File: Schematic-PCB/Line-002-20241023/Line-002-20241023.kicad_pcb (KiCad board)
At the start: 2 copper layers, 195 x 192.8 mm, 217 parts, among them U53 ATmega2560-16A

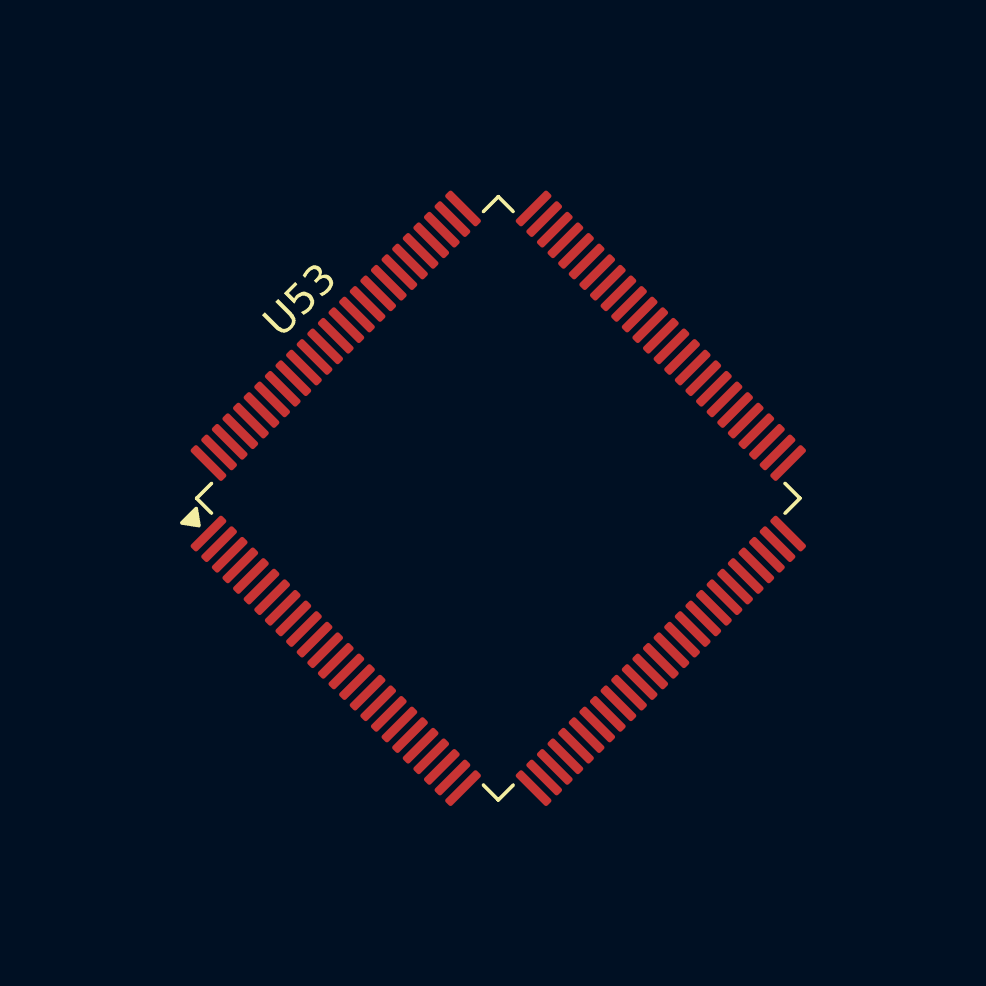
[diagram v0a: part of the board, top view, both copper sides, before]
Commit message: update: ラインセンサ ver.002 の回路図を進めた
コンパレータを追加
ピンアサインはちょっと悩み中だけどほぼいい感じだと思う...たぶん。
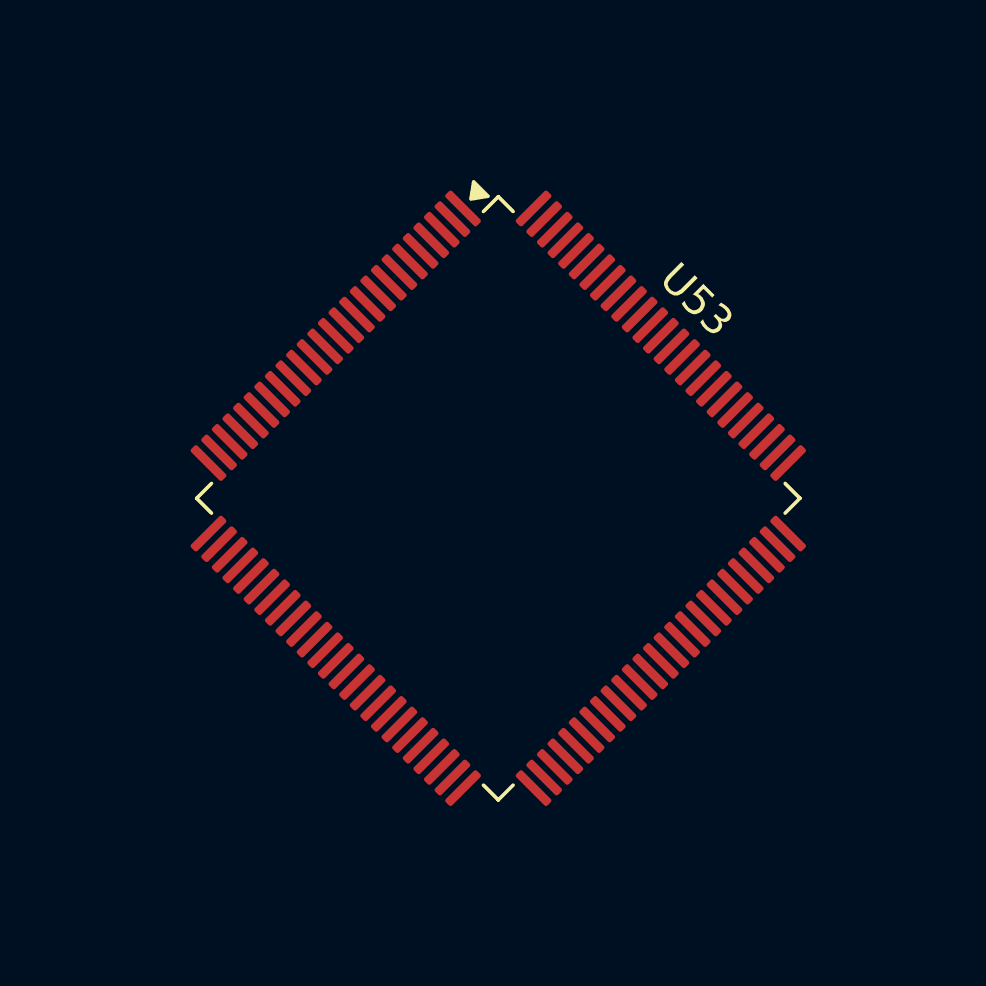
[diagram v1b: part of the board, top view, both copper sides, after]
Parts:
- turned U53 to -45 degrees

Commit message: add: update: ラインセンサ基板の外形の更新版を追加 & PCBデザイン/回路図を進めた
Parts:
- removed R100, R101, R102, R103, R104, R92, R93, R94, R95, R96, R97, R98, R99: 75, Resistor_SMD:R_0603_1608Metric
- removed R105: 10K, Resistor_SMD:R_0603_1608Metric
- removed R106, R107, R108: 330, Resistor_SMD:R_0603_1608Metric
- removed U46, U47, U48, U49, U50, U51, U52: ~, @2024TOINIOT2-Line:NJL7502L
- removed U53: ATmega2560-16A, Package_QFP:TQFP-100_14x14mm_P0.5mm
- added C1: 100nF, Capacitor_SMD:C_0603_1608Metric, F.Cu at (203.2, 62.1)
- added C2: 100nF, Capacitor_SMD:C_0603_1608Metric, F.Cu at (203.2, 64.6)
- added C3: 22pF, Capacitor_SMD:C_0603_1608Metric, F.Cu at (203.2, 67.1)
- added C4: 22pF, Capacitor_SMD:C_0603_1608Metric, F.Cu at (203.2, 69.6)
- added C5: 100nF, Capacitor_SMD:C_0603_1608Metric, F.Cu at (203.2, 72.1)
- added C6: 22pF, Capacitor_SMD:C_0603_1608Metric, F.Cu at (203.2, 74.6)
- added C7: 100nF, Capacitor_SMD:C_0603_1608Metric, F.Cu at (203.2, 77.1)
- added C8: 1000uF, Capacitor_SMD:C_0603_1608Metric, F.Cu at (203.2, 79.7)
- added C9: 10uF, Capacitor_SMD:C_0805_2012Metric, F.Cu at (203.5, 110.7)
- added D56: PWR, LED_SMD:LED_0603_1608Metric, F.Cu at (229.5, 113.2)
- added J1: ICSP, Connector_PinHeader_2.54mm:PinHeader_2x03_P2.54mm_Vertical, F.Cu at (249.7, 106.4)
- added J2: VIN, Connector_JST:JST_VH_B2P-VH-B_1x02_P3.96mm_Vertical, F.Cu at (-12.0, 29.9)
- added JP1: 160Hz, Jumper:SolderJumper-2_P1.3mm_Open_Pad1.0x1.5mm, F.Cu at (229.7, 95.2)
- added JP2: 16Hz, Jumper:SolderJumper-2_P1.3mm_Open_Pad1.0x1.5mm, F.Cu at (229.7, 98.8)
- added JP3: 1.6Hz, Jumper:SolderJumper-2_P1.3mm_Open_Pad1.0x1.5mm, F.Cu at (229.7, 102.3)
- added Y1: 16MHz, @2024TOINIOT2-Line:AL4BT, F.Cu at (239.4, 110.5)
- D25, D26, D27, D28, D29, U25, U26, U27, U28, U29: moved to B.Cu
- R29, R30, R31, R32, R33, R34, R35, R36, R37, R38, R39, R40, R41, R42, R43, R44, R45, R46, R47, R48, R49, R50, R51, R52: value Line-PDWN -> 75
- R81, R82, R87, R90: value 75 -> 10K
- R83, R84, R85, R91: value 75 -> 330
- R86: value 75 -> 1M
- R88: value 75 -> 100
- R89: value 75 -> 1K
- U45: value ~ -> ATmega2560-16A; footprint @2024TOINIOT2-Line:NJL7502L -> Package_QFP:TQFP-100_14x14mm_P0.5mm
- moved U25 283.0 mm to (-22.5, -87.4), turned to 50 degrees
- moved U26 275.2 mm to (-12.0, -81.3), turned to 70 degrees
- moved U27 269.7 mm to (-0.00, -79.2), turned to 90 degrees
- moved U29 236.8 mm to (22.5, -87.4), turned to 130 degrees
- moved U28 235.7 mm to (12.0, -81.3), turned to 110 degrees
- moved D25 215.3 mm to (-25.7, -83.5), turned to -130 degrees
- moved D26 206.7 mm to (-13.7, -76.6), turned to -110 degrees
- moved D27 201.4 mm to (-0.00, -74.2), turned to -90 degrees
- moved U45 196.4 mm to (7.50, 41.0), turned to -45 degrees
- moved D29 166.2 mm to (25.7, -83.5), turned to -50 degrees
- moved D28 163.1 mm to (13.7, -76.6), turned to -70 degrees
- moved D36 129.8 mm to (241.5, 63.5)
- moved D42 126.9 mm to (246.9, 63.5)
- moved D43 126.9 mm to (246.9, 69.0)
- moved D44 126.9 mm to (246.9, 74.5)
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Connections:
- R25 pad 1: Line-F-01 -> Line-F
- R26 pad 1: Line-F-02 -> Line-L
- R27 pad 1: Line-F-03 -> Line-B
- R28 pad 1: Line-F-04 -> Line-R
- R29 pad 1: Line-F-05 -> +5V
- R29 pad 2: GND -> Net-(D1-A)
- R30 pad 1: Line-F-06 -> +5V
- R30 pad 2: GND -> Net-(D2-A)
- R31 pad 1: Line-F-07 -> +5V
- R31 pad 2: GND -> Net-(D3-A)
- R32 pad 1: Line-L-01 -> +5V
- R32 pad 2: GND -> Net-(D4-A)
- R33 pad 1: Line-L-02 -> +5V
- R33 pad 2: GND -> Net-(D5-A)
- R34 pad 1: Line-L-03 -> +5V
- R34 pad 2: GND -> Net-(D6-A)
- R35 pad 1: Line-L-04 -> +5V
- R35 pad 2: GND -> Net-(D7-A)
- R36 pad 1: Line-L-05 -> +5V
- R36 pad 2: GND -> Net-(D8-A)
- R37 pad 1: Line-L-06 -> +5V
- R37 pad 2: GND -> Net-(D9-A)
- R38 pad 1: Line-L-07 -> +5V
- R38 pad 2: GND -> Net-(D10-A)
- R39 pad 1: Line-B-01 -> +5V
- R39 pad 2: GND -> Net-(D11-A)
- R40 pad 1: Line-B-02 -> +5V
- R40 pad 2: GND -> Net-(D12-A)
- R41 pad 1: Line-B-03 -> +5V
- R41 pad 2: GND -> Net-(D13-A)
- R42 pad 1: Line-B-04 -> +5V
- R42 pad 2: GND -> Net-(D14-A)
- R43 pad 1: Line-B-05 -> +5V
- R43 pad 2: GND -> Net-(D15-A)
- R44 pad 1: Line-B-06 -> +5V
- R44 pad 2: GND -> Net-(D16-A)
- R45 pad 1: Line-B-07 -> +5V
- R45 pad 2: GND -> Net-(D17-A)
- R46 pad 1: Line-R-01 -> +5V
- R46 pad 2: GND -> Net-(D18-A)
- R47 pad 1: Line-R-02 -> +5V
- R47 pad 2: GND -> Net-(D19-A)
- R48 pad 1: Line-R-03 -> +5V
- R48 pad 2: GND -> Net-(D20-A)
- R49 pad 1: Line-R-04 -> +5V
- R49 pad 2: GND -> Net-(D21-A)
- R50 pad 1: Line-R-05 -> +5V
- R50 pad 2: GND -> Net-(D22-A)
- R51 pad 1: Line-R-06 -> +5V
- R51 pad 2: GND -> Net-(D23-A)
- R52 pad 1: Line-R-07 -> +5V
- R52 pad 2: GND -> Net-(D24-A)
- R53 pad 2: Net-(D1-A) -> Net-(D25-A)
- R54 pad 2: Net-(D2-A) -> Net-(D26-A)
- R55 pad 2: Net-(D3-A) -> Net-(D27-A)
- R56 pad 2: Net-(D4-A) -> Net-(D28-A)
- R57 pad 2: Net-(D5-A) -> Net-(D29-A)
- R58 pad 2: Net-(D6-A) -> Net-(D30-A)
- R59 pad 2: Net-(D7-A) -> Net-(D31-A)
- R60 pad 2: Net-(D8-A) -> Net-(D32-A)
- R61 pad 2: Net-(D9-A) -> Net-(D33-A)
- R62 pad 2: Net-(D10-A) -> Net-(D34-A)
- R63 pad 2: Net-(D11-A) -> Net-(D35-A)
- R64 pad 2: Net-(D12-A) -> Net-(D36-A)
- R65 pad 2: Net-(D13-A) -> Net-(D37-A)
- R66 pad 2: Net-(D14-A) -> Net-(D38-A)
- R67 pad 2: Net-(D15-A) -> Net-(D39-A)
- R68 pad 2: Net-(D16-A) -> Net-(D40-A)
- R69 pad 2: Net-(D17-A) -> Net-(D41-A)
- R70 pad 2: Net-(D18-A) -> Net-(D42-A)
- R71 pad 2: Net-(D19-A) -> Net-(D43-A)
- R72 pad 2: Net-(D20-A) -> Net-(D44-A)
- R73 pad 2: Net-(D21-A) -> Net-(D45-A)
- R74 pad 2: Net-(D22-A) -> Net-(D46-A)
- R75 pad 2: Net-(D23-A) -> Net-(D47-A)
- R76 pad 2: Net-(D24-A) -> Net-(D48-A)
- R77 pad 2: Net-(D25-A) -> Net-(D49-A)
- R78 pad 2: Net-(D26-A) -> Net-(D50-A)
- R79 pad 2: Net-(D27-A) -> Net-(D51-A)
- R80 pad 2: Net-(D28-A) -> Net-(D52-A)
- R81 pad 2: Net-(D29-A) -> RESET
- R82 pad 2: Net-(D30-A) -> SDA
- R83 pad 1: +5V -> LED01
- R83 pad 2: Net-(D31-A) -> Net-(D53-A)
- R84 pad 1: +5V -> LED02
- R84 pad 2: Net-(D32-A) -> Net-(D54-A)
- R85 pad 1: +5V -> LED03
- R85 pad 2: Net-(D33-A) -> Net-(D55-A)
- R86 pad 1: +5V -> XTAL1
- R86 pad 2: Net-(D34-A) -> XTAL2
- R87 pad 2: Net-(D35-A) -> SCL
- R88 pad 1: +5V -> Net-(JP1-B)
- R88 pad 2: Net-(D36-A) -> Threshold
- R89 pad 1: +5V -> Net-(JP2-B)
- R89 pad 2: Net-(D37-A) -> Threshold
- R90 pad 1: +5V -> Net-(JP3-B)
- R90 pad 2: Net-(D38-A) -> Threshold
- R91 pad 1: +5V -> Net-(D56-A)
- R91 pad 2: Net-(D39-A) -> +5V
- U25 pad 1: Line-F-01 -> Line-F
- U26 pad 1: Line-F-02 -> Line-F
- U27 pad 1: Line-F-03 -> Line-F
- U28 pad 1: Line-F-04 -> Line-F
- U29 pad 1: Line-F-05 -> Line-F
- U30 pad 1: Line-F-06 -> Line-L
- U31 pad 1: Line-F-07 -> Line-L
- U32 pad 1: Line-L-01 -> Line-L
- U33 pad 1: Line-L-02 -> Line-L
- U34 pad 1: Line-L-03 -> Line-L
- U35 pad 1: Line-L-04 -> Line-B
- U36 pad 1: Line-L-05 -> Line-B
- U37 pad 1: Line-L-06 -> Line-B
- U38 pad 1: Line-L-07 -> Line-B
- U39 pad 1: Line-B-01 -> Line-B
- U40 pad 1: Line-B-02 -> Line-R
- U41 pad 1: Line-B-03 -> Line-R
- U42 pad 1: Line-B-04 -> Line-R
- U43 pad 1: Line-B-05 -> Line-R
- U44 pad 1: Line-B-06 -> Line-R
- U45 pad 1: Line-B-07 -> PWM
- U45 pad 2: +5V -> RX0
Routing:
- added copper zone on B.Cu, net GND
- added copper zone on F.Cu, net GND
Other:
- board size 195 x 192.8 mm -> 195 x 191.1 mm
- copper layers 2 -> 4

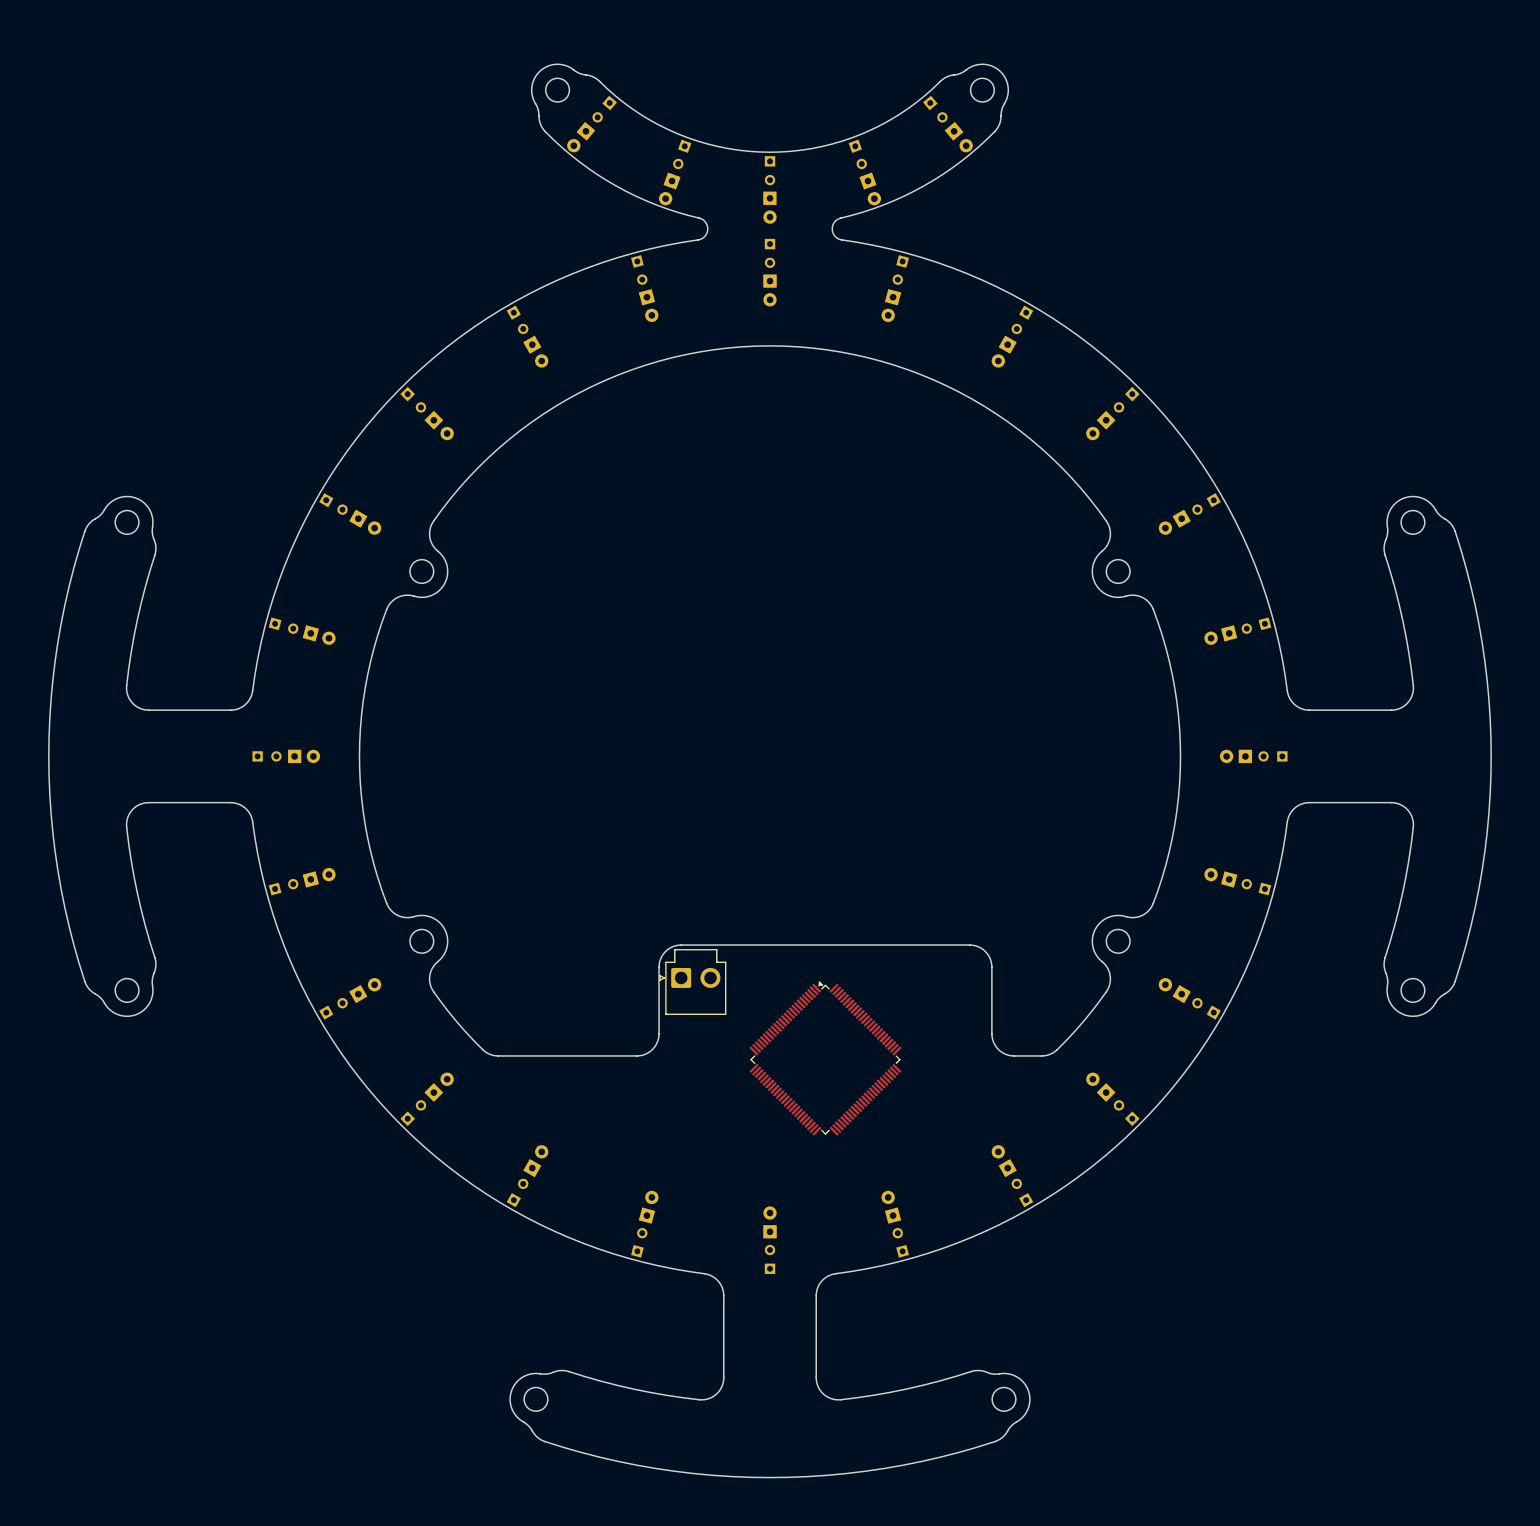
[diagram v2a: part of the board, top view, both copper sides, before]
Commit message: update: ラインセンサ基板の基板外形を更新した
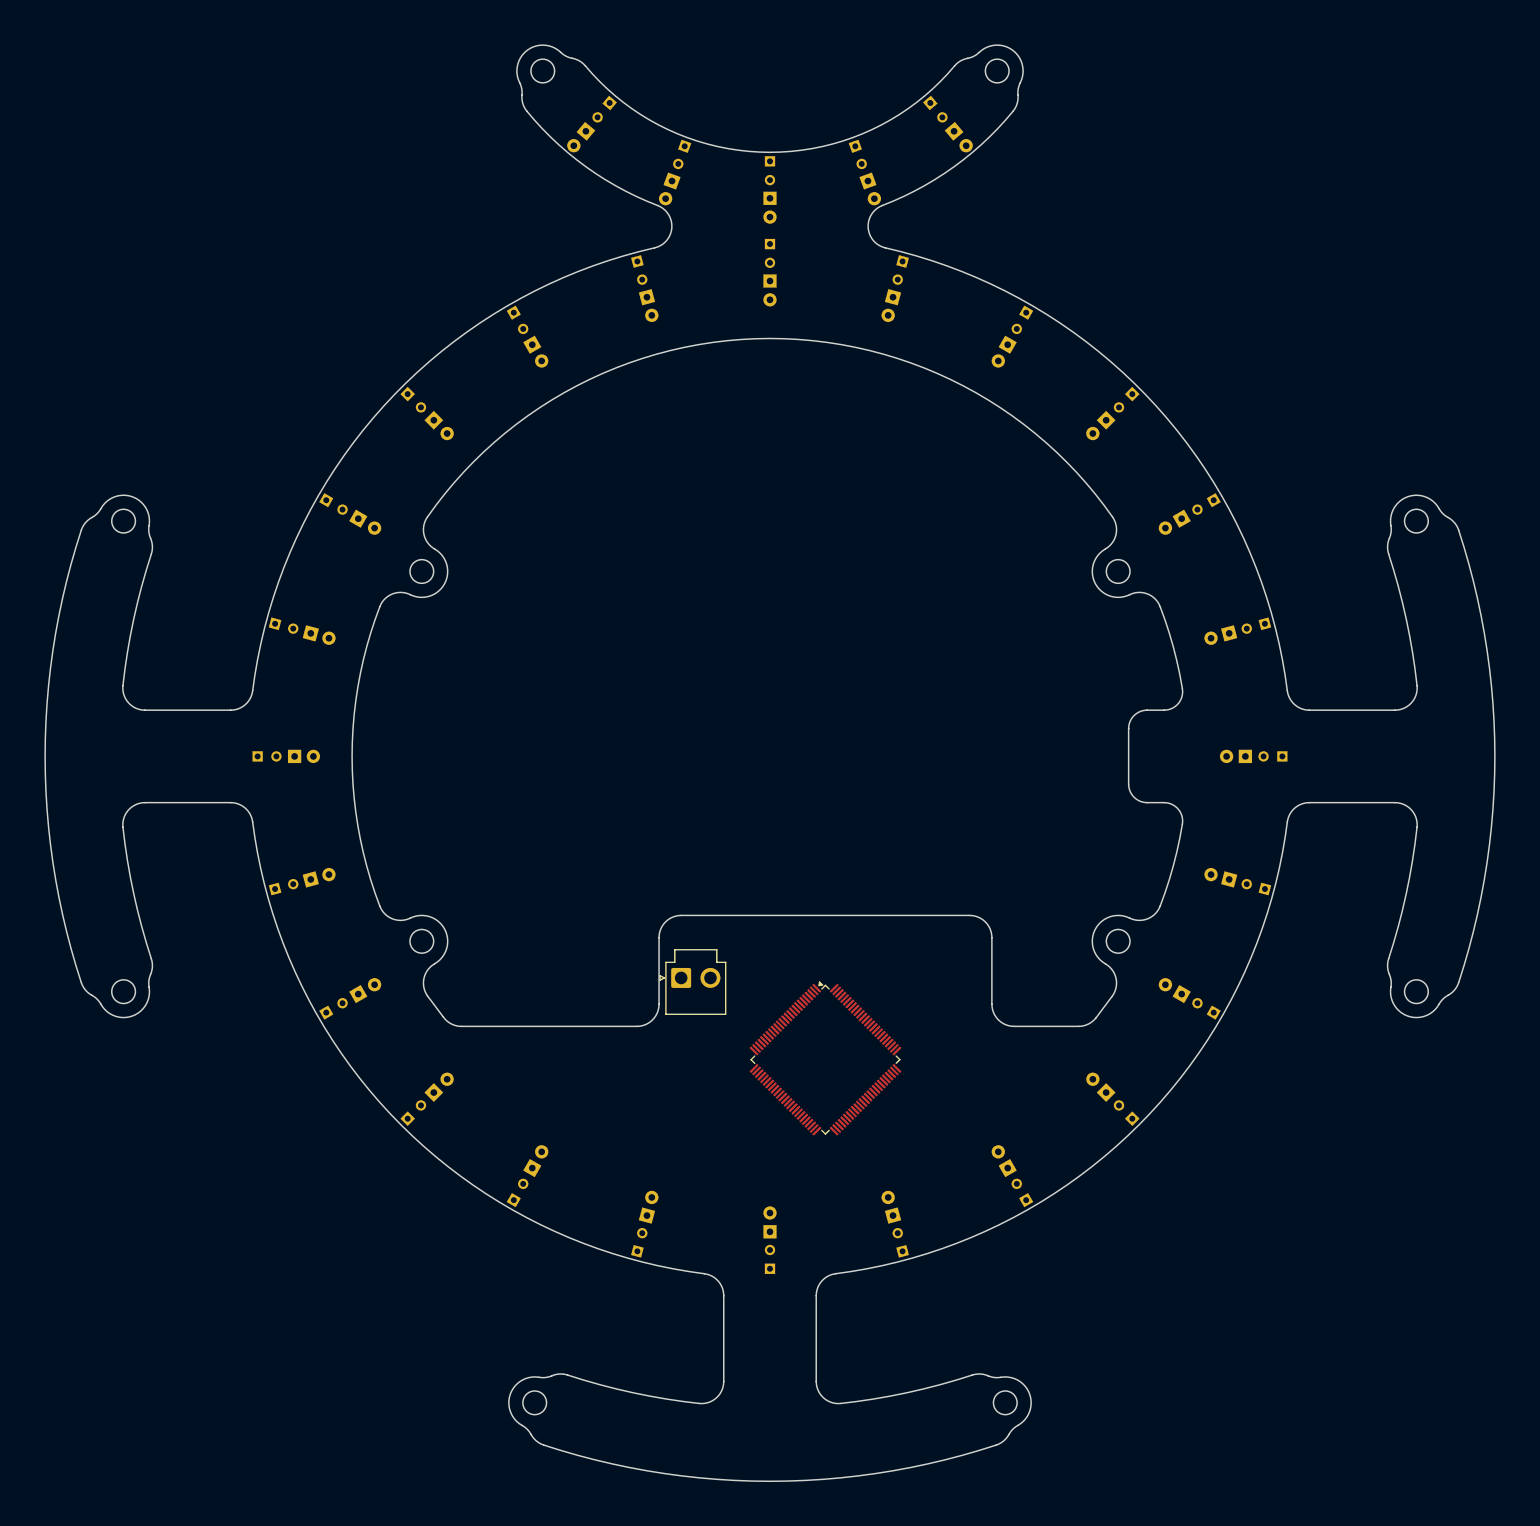
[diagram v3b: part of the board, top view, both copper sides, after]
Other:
- board size 195 x 191.1 mm -> 196 x 194.2 mm

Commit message: update: ラインセンサ基板のPCBを進めた
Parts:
- added REF**: MountingHole_3.2mm_M3, MountingHole:MountingHole_3.2mm_M3, F.Cu at (-31.8, 87.4)
- added REF**: MountingHole_3.2mm_M3, MountingHole:MountingHole_3.2mm_M3, F.Cu at (-87.4, -31.8)
- added REF**: MountingHole_3.2mm_M3, MountingHole:MountingHole_3.2mm_M3, F.Cu at (30.7, -92.7)
- added REF**: MountingHole_3.2mm_M3, MountingHole:MountingHole_3.2mm_M3, F.Cu at (87.4, -31.8)
- added REF**: MountingHole_3.2mm_M3, MountingHole:MountingHole_3.2mm_M3, F.Cu at (-30.7, -92.7)
- added REF**: MountingHole_3.2mm_M3, MountingHole:MountingHole_3.2mm_M3, F.Cu at (87.4, 31.8)
- added REF**: MountingHole_3.2mm_M3, MountingHole:MountingHole_3.2mm_M3, F.Cu at (47.1, 25.0)
- added REF**: MountingHole_3.2mm_M3, MountingHole:MountingHole_3.2mm_M3, F.Cu at (-47.1, 25.0)
- added REF**: MountingHole_3.2mm_M3, MountingHole:MountingHole_3.2mm_M3, F.Cu at (31.8, 87.4)
- added REF**: MountingHole_3.2mm_M3, MountingHole:MountingHole_3.2mm_M3, F.Cu at (-87.4, 31.8)
- added REF**: MountingHole_3.2mm_M3, MountingHole:MountingHole_3.2mm_M3, F.Cu at (-47.1, -25.0)
- moved D7 126.0 mm to (63.0, 0.00), turned to 180 degrees
- moved D19 126.0 mm to (-63.0, 0.00), turned to 0 degrees
- moved D6 121.7 mm to (60.9, -16.3), turned to -165 degrees
- moved D8 121.7 mm to (60.9, 16.3), turned to 165 degrees
- moved D18 121.7 mm to (-60.9, 16.3), turned to 15 degrees
- moved D20 121.7 mm to (-60.9, -16.3), turned to -15 degrees
- moved D5 109.1 mm to (54.6, -31.5), turned to -150 degrees
- moved D9 109.1 mm to (54.6, 31.5), turned to 150 degrees
- moved D17 109.1 mm to (-54.6, 31.5), turned to 30 degrees
- moved D21 109.1 mm to (-54.6, -31.5), turned to -30 degrees
- moved D10 89.1 mm to (44.5, 44.5), turned to 135 degrees
- moved D4 89.1 mm to (44.5, -44.5), turned to -135 degrees
- moved D22 89.1 mm to (-44.5, -44.5), turned to -45 degrees
- moved D16 89.1 mm to (-44.5, 44.5), turned to 45 degrees
- moved D11 63.0 mm to (31.5, 54.6), turned to 120 degrees
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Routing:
- net Line-F: track 0.00 -> 46.8 mm
- added copper zone on In1.Cu, net +5V
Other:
- outline, holes or cut-outs redrawn
